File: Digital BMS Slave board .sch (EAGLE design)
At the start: 252 parts, among them J1 S4B-PH-K, J10 S3B-PH-K, J11 S6B-PH-K, J12 MOLEX22-12-406205-7068, J2 S4B-PH-K, J3 S4B-PH-K, J4 S4B-PH-K, J5 S2B-PH-K, J6 S2B-PH-K, J7 S2B-PH-K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

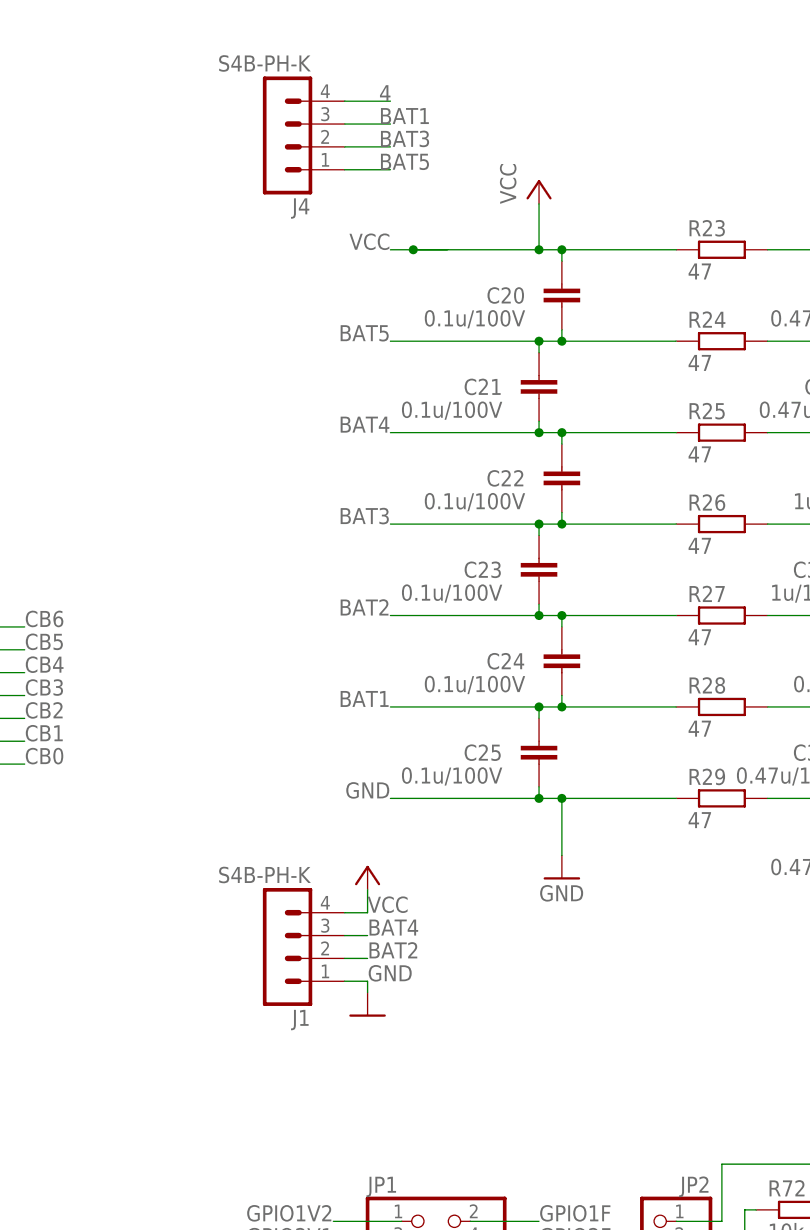
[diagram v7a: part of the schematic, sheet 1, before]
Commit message: Test rings for voltage sensing added
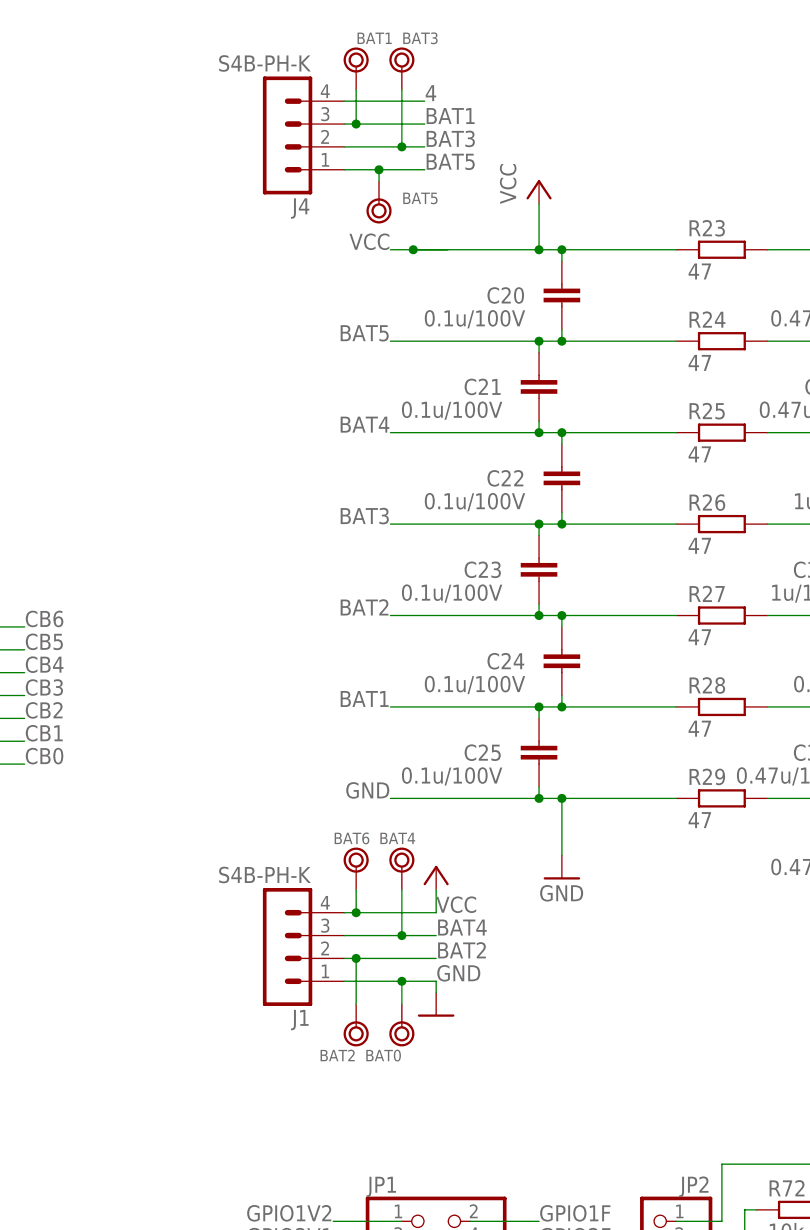
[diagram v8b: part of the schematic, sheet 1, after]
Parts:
- removed GND: 5000, testing:5000
- added BAT0, BAT1, BAT2, BAT3, BAT4, BAT5, BAT6, TP1: TEST_RING, testing:TEST_RING
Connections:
- net BAT1: now also BAT1.P$1
- net BAT2: now also BAT2.P$1
- net BAT3: now also BAT3.P$1
- net BAT4: now also BAT4.P$1
- net BAT5: now also BAT5.P$1
- net GND: now also BAT0.P$1
- net N$11: now also TP1.P$1; no longer GND.1
- net VCC: now also BAT6.P$1
